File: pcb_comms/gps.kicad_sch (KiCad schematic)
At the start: 22 parts, among them U1 MAX-M10S-00B

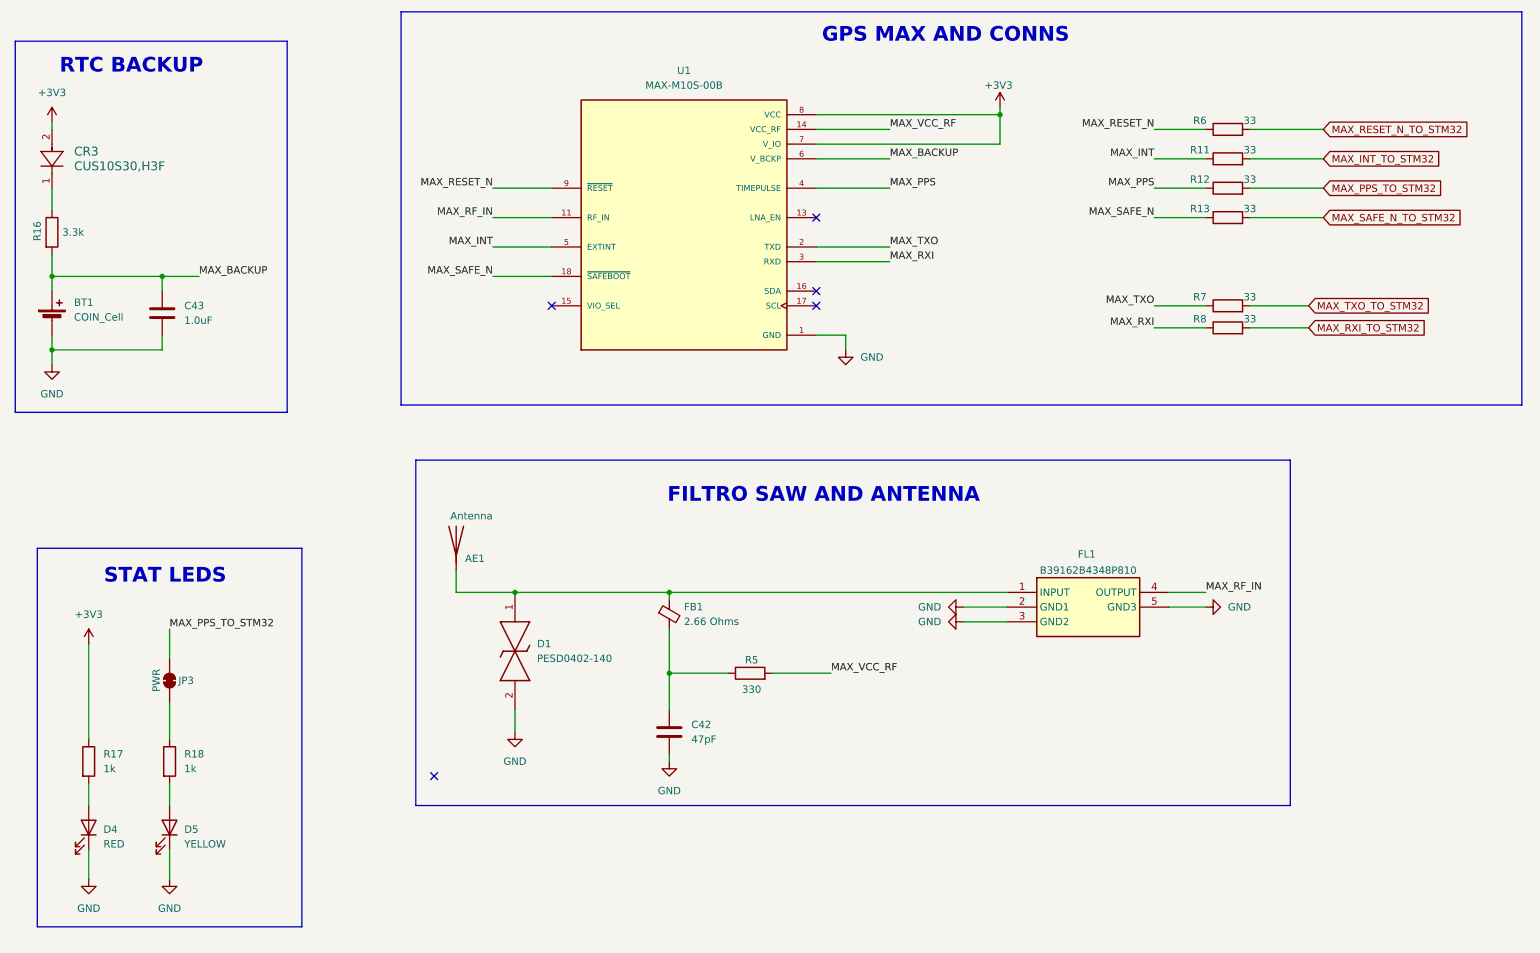
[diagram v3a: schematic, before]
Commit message: Add antenna deploy
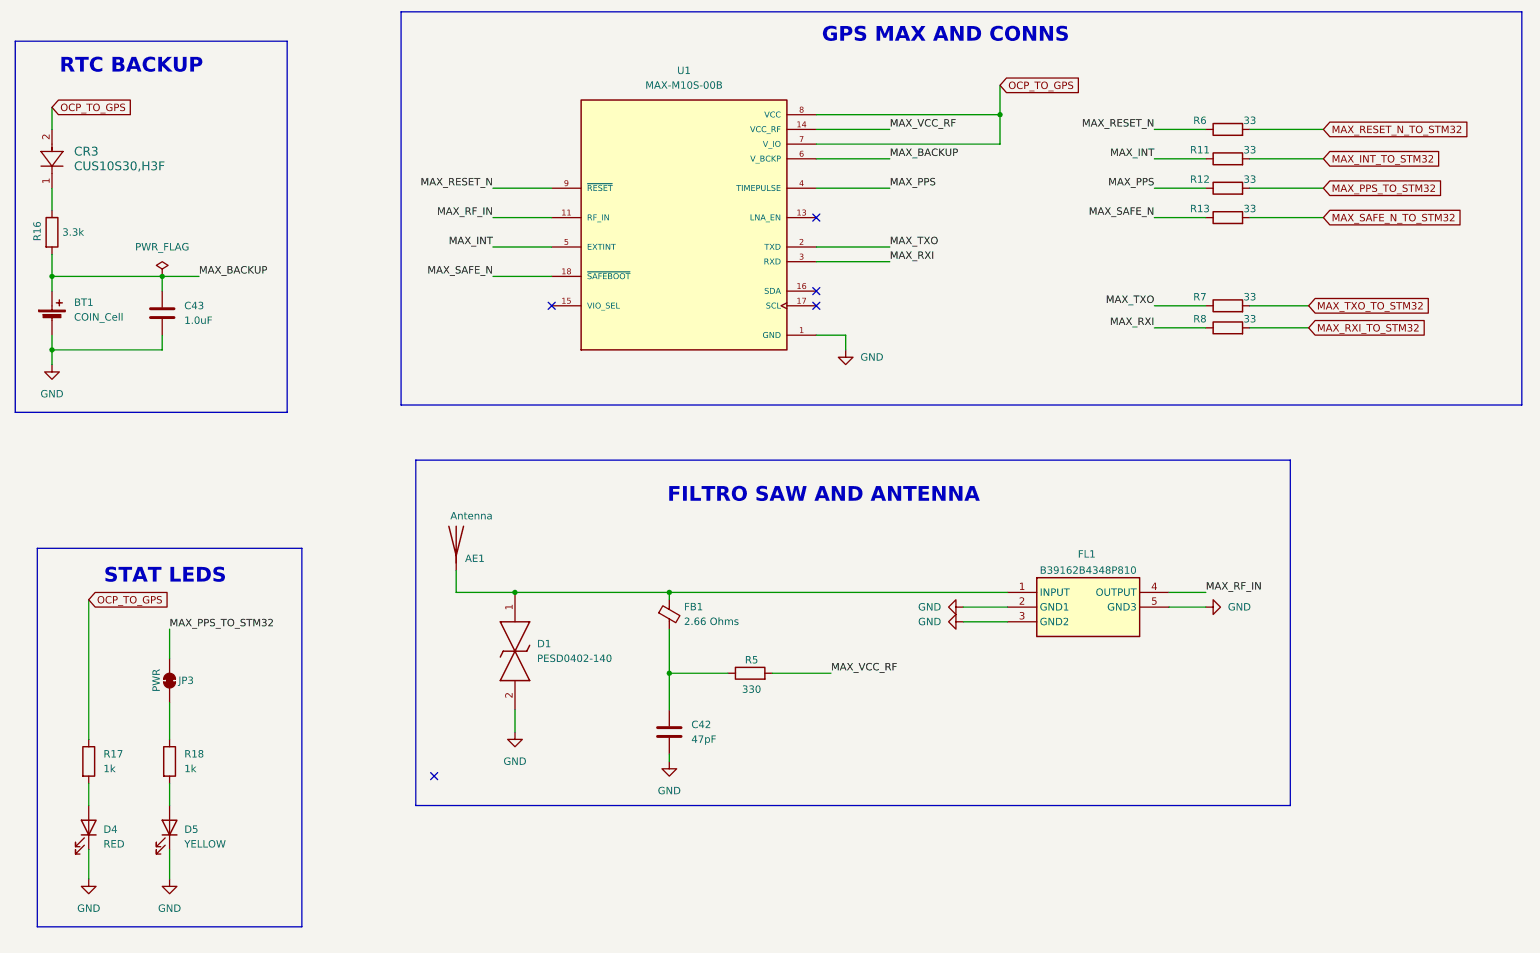
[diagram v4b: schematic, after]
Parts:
- D1: footprint DIONC1005X43N -> (none)
- FL1: footprint B39162B4348P810 -> (none)
- U1: footprint (none) -> MAX-M10S-00B:XCVR_MAX-M10S-00B
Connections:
- net +3V3 renamed OCP_TO_GPS
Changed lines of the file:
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@@
 	(wire
 		(pts
+			(xy 30.48 124.46) (xy 30.48 148.59)
+		)
+		(stroke
+			(width 0)
+			(type default)
+		)
+	)
+	(wire
+		(pts
 			(xy 187.96 45.72) (xy 187.96 40.64)
 		)
@@
 	(wire
 		(pts
-			(xy 24.13 41.91) (xy 24.13 43.18)
+			(xy 24.13 39.37) (xy 24.13 43.18)
 		)
 		(stroke
@@
 	(wire
 		(pts
-			(xy 187.96 40.64) (xy 187.96 39.37)
+			(xy 187.96 40.64) (xy 187.96 35.56)
 		)
 		(stroke
@@
 	(wire
 		(pts
-			(xy 30.48 132.08) (xy 30.48 148.59)
-		)
-		(stroke
-			(width 0)
-			(type default)
-		)
-	)
-	(wire
-		(pts
 			(xy 104.14 123.19) (xy 93.98 123.19)
 		)
@@
 		)
 	)
+	(global_label "OCP_TO_GPS"
+		(shape input)
+		(at 187.96 35.56 0)
+		(fields_autoplaced yes)
+		(effects
+			(font
+				(size 1.27 1.27)
+			)
+			(justify left)
+		)
+		(property "Intersheetrefs" "${INTERSHEET_REFS}"
+			(at 202.7985 35.56 0)
+			(effects
+				(font
+					(size 1.27 1.27)
+				)
+				(justify left)
+				(hide yes)
+			)
+		)
+	)
 	(global_label "MAX_PPS_TO_STM32"
 		(shape input)
@@
 		)
 	)
+	(global_label "OCP_TO_GPS"
+		(shape input)
+		(at 30.48 124.46 0)
+		(fields_autoplaced yes)
+		(effects
+			(font
+				(size 1.27 1.27)
+			)
+			(justify left)
+		)
+		(property "Intersheetrefs" "${INTERSHEET_REFS}"
+			(at 45.3185 124.46 0)
+			(effects
+				(font
+					(size 1.27 1.27)
+				)
+				(justify left)
+				(hide yes)
+			)
+		)
+	)
+	(global_label "OCP_TO_GPS"
+		(shape input)
+		(at 24.13 39.37 0)
+		(fields_autoplaced yes)
+		(effects
+			(font
+				(size 1.27 1.27)
+			)
+			(justify left)
+		)
+		(property "Intersheetrefs" "${INTERSHEET_REFS}"
+			(at 38.9685 39.37 0)
+			(effects
+				(font
+					(size 1.27 1.27)
+				)
+				(justify left)
+				(hide yes)
+			)
+		)
+	)
 	(global_label "MAX_TXO_TO_STM32"
 		(shape input)
@@
 	)
 	(symbol
+		(lib_id "power:PWR_FLAG")
+		(at 43.18 68.58 0)
+		(unit 1)
+		(exclude_from_sim no)
+		(in_bom yes)
+		(on_board yes)
+		(dnp no)
+		(fields_autoplaced yes)
+		(property "Reference" "#FLG07"
+			(at 43.18 66.675 0)
+			(effects
+				(font
+					(size 1.27 1.27)
+				)
+				(hide yes)
+			)
+		)
+		(property "Value" "PWR_FLAG"
+			(at 43.18 63.5 0)
+			(effects
+				(font
+					(size 1.27 1.27)
+				)
+			)
+		)
+		(property "Footprint" ""
+			(at 43.18 68.58 0)
+			(effects
+				(font
+					(size 1.27 1.27)
+				)
+				(hide yes)
+			)
+		)
+		(property "Datasheet" "~"
+			(at 43.18 68.58 0)
+			(effects
+				(font
+					(size 1.27 1.27)
+				)
+				(hide yes)
+			)
+		)
+		(property "Description" "Special symbol for telling ERC where power comes from"
+			(at 43.18 68.58 0)
+			(effects
+				(font
+					(size 1.27 1.27)
+				)
+				(hide yes)
+			)
+		)
+		(pin "1"
+		)
+		(instances
+			(project ""
+				(path "/ea597178-b44d-4db9-826c-8f86e8d231f0/9ced98fe-3695-442f-a613-f1ea774ec3ca"
+					(reference "#FLG07")
+					(unit 1)
+				)
+			)
+		)
+	)
+	(symbol
 		(lib_id "Device:R")
 		(at 144.78 137.16 90)
@@
 			)
 		)
-		(property "Footprint" "B39162B4348P810"
+		(property "Footprint" ""
 			(at 257.81 220.65 0)
 			(effects
@@
 			)
 		)
-		(property "Footprint" "DIONC1005X43N"
+		(property "Footprint" ""
 			(at 10.49 135.89 0)
 			(effects
@@
 			)
 		)
-		(property "Footprint" ""
+		(property "Footprint" "MAX-M10S-00B:XCVR_MAX-M10S-00B"
 			(at 133.35 58.42 0)
 			(effects
@@
 	)
 	(symbol
-		(lib_id "power:+3V3")
-		(at 24.13 41.91 0)
-		(unit 1)
-		(exclude_from_sim no)
-		(in_bom yes)
-		(on_board yes)
-		(dnp no)
-		(fields_autoplaced yes)
-		(property "Reference" "#PWR052"
-			(at 24.13 45.72 0)
-			(effects
-				(font
-					(size 1.27 1.27)
-				)
-				(hide yes)
-			)
-		)
-		(property "Value" "+3V3"
-			(at 24.13 36.83 0)
-			(effects
-				(font
-					(size 1.27 1.27)
-				)
-			)
-		)
-		(property "Footprint" ""
-			(at 24.13 41.91 0)
-			(effects
-				(font
-					(size 1.27 1.27)
-				)
-				(hide yes)
-			)
-		)
-		(property "Datasheet" ""
-			(at 24.13 41.91 0)
-			(effects
-				(font
-					(size 1.27 1.27)
-				)
-				(hide yes)
-			)
-		)
-		(property "Description" "Power symbol creates a global label with name \"+3V3\""
-			(at 24.13 41.91 0)
-			(effects
-				(font
-					(size 1.27 1.27)
-				)
-				(hide yes)
-			)
-		)
-		(pin "1"
-		)
-		(instances
-			(project ""
-				(path "/ea597178-b44d-4db9-826c-8f86e8d231f0/9ced98fe-3695-442f-a613-f1ea774ec3ca"
-					(reference "#PWR052")
-					(unit 1)
-				)
-			)
-		)
-	)
-	(symbol
 		(lib_id "Device:R")
 		(at 227.33 58.42 90)
@@
 	)
 	(symbol
-		(lib_id "power:+3V3")
-		(at 30.48 132.08 0)
-		(unit 1)
-		(exclude_from_sim no)
-		(in_bom yes)
-		(on_board yes)
-		(dnp no)
-		(fields_autoplaced yes)
-		(property "Reference" "#PWR054"
-			(at 30.48 135.89 0)
-			(effects
-				(font
-					(size 1.27 1.27)
-				)
-				(hide yes)
-			)
-		)
-		(property "Value" "+3V3"
-			(at 30.48 127 0)
-			(effects
-				(font
-					(size 1.27 1.27)
-				)
-			)
-		)
-		(property "Footprint" ""
-			(at 30.48 132.08 0)
-			(effects
-				(font
-					(size 1.27 1.27)
-				)
-				(hide yes)
-			)
-		)
-		(property "Datasheet" ""
-			(at 30.48 132.08 0)
-			(effects
-				(font
-					(size 1.27 1.27)
-				)
-				(hide yes)
-			)
-		)
-		(property "Description" "Power symbol creates a global label with name \"+3V3\""
-			(at 30.48 132.08 0)
-			(effects
-				(font
-					(size 1.27 1.27)
-				)
-				(hide yes)
-			)
-		)
-		(pin "1"
-		)
-		(instances
-			(project "pcb_comms_board"
-				(path "/ea597178-b44d-4db9-826c-8f86e8d231f0/9ced98fe-3695-442f-a613-f1ea774ec3ca"
-					(reference "#PWR054")
-					(unit 1)
-				)
-			)
-		)
-	)
-	(symbol
 		(lib_id "power:GND")
 		(at 223.52 125.73 90)
@@
 					(unit 1)
 				)
-			)
-		)
-	)
-	(symbol
-		(lib_id "power:+3V3")
-		(at 187.96 39.37 0)
-		(unit 1)
-		(exclude_from_sim no)
-		(in_bom yes)
-		(on_board yes)
-		(dnp no)
-		(property "Reference" "#PWR044"
-			(at 187.96 43.18 0)
-			(effects
-				(font
-					(size 1.27 1.27)
-				)
-				(hide yes)
-			)
-		)
-		(property "Value" "+3V3"
-			(at 187.706 35.56 0)
-			(effects
-				(font
-					(size 1.27 1.27)
-				)
-			)
-		)
-		(property "Footprint" ""
-			(at 187.96 39.37 0)
-			(effects
-				(font
-					(size 1.27 1.27)
-				)
-				(hide yes)
-			)
-		)
-		(property "Datasheet" ""
-			(at 187.96 39.37 0)
-			(effects
-				(font
-					(size 1.27 1.27)
-				)
-				(hide yes)
-			)
-		)
-		(property "Description" "Power symbol creates a global label with name \"+3V3\""
-			(at 187.96 39.37 0)
-			(effects
-				(font
-					(size 1.27 1.27)
-				)
-				(hide yes)
-			)
-		)
-		(pin "1"
-		)
-		(instances
-			(project ""
-				(path "/ea597178-b44d-4db9-826c-8f86e8d231f0/9ced98fe-3695-442f-a613-f1ea774ec3ca"
-					(reference "#PWR044")
-					(unit 1)
-				)

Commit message: Last update
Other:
- company: (none) -> Sanie Peralta, Alejandro Campo
- title: (none) -> PC1: APRS & GPS
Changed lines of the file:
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@@
 	(generator_version "9.0")
 	(paper "A4")
+	(title_block
+		(title "PC1: APRS & GPS")
+		(date "2026-04-01")
+		(rev "1.0")
+		(company "Sanie Peralta, Alejandro Campo")
+		(comment 1 "Introducción a la Ingeniería Satelital ")
+		(comment 2 "Primer Parcial")
+	)
 	(text "GPS MAX AND CONNS"
 		(exclude_from_sim no)

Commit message: rev 1.1
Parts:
- removed AE1: Antenna, symbol Device:Antenna
- added AE2: Antenna_Shield, symbol Device:Antenna_Shield
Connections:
- net GND: now also AE2.2 (Shield)
- net at D1.1, FB1.1, FL1.1 (INPUT): now also AE2.1 (A)
- no-connect marks 5 -> 4
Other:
- moved on the sheet: D4, D5, FB1, JP3, R17, R18

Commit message: Finish schematic
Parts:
- U1: footprint MAX-M10S-00B:XCVR_MAX-M10S-00B -> (none)
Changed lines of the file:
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@@
 	(wire
 		(pts
-			(xy 48.26 132.08) (xy 48.26 137.16)
+			(xy 48.26 130.81) (xy 48.26 137.16)
 		)
 		(stroke
@@
 		)
 	)
-	(label "MAX_PPS_TO_STM32"
-		(at 48.26 132.08 0)
-		(effects
-			(font
-				(size 1.27 1.27)
-			)
-			(justify left bottom)
-		)
-	)
 	(label "MAX_PPS"
 		(at 168.91 53.34 0)
@@
 			)
 			(justify right bottom)
+		)
+	)
+	(global_label "MAX_PPS_TO_STM32"
+		(shape input)
+		(at 48.26 130.81 0)
+		(fields_autoplaced yes)
+		(effects
+			(font
+				(size 1.27 1.27)
+			)
+			(justify left)
+		)
+		(property "Intersheetrefs" "${INTERSHEET_REFS}"
+			(at 69.9926 130.81 0)
+			(effects
+				(font
+					(size 1.27 1.27)
+				)
+				(justify left)
+				(hide yes)
+			)
 		)
 	)
@@
 			)
 		)
-		(property "Footprint" "MAX-M10S-00B:XCVR_MAX-M10S-00B"
+		(property "Footprint" ""
 			(at 133.35 58.42 0)
 			(effects

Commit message: Version 1.0. No DRA yet
From now on I will make the connections for IIS and then adapt it for the club
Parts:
- C43: value 1.0uF -> 1uF
- FB1: value 2.66 Ohms -> 2.66R
- R11, R12, R13, R6, R7, R8: value 33 -> 33R
- R16: value 3.3k -> 3.3K
- R17, R18: value 1k -> 1K
- R5: value 330 -> 330R
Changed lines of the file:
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@@
 			)
 		)
-		(property "Value" "2.66 Ohms"
+		(property "Value" "2.66R"
 			(at 133.35 130.7718 0)
 			(effects
@@
 			)
 		)
-		(property "Value" "330"
+		(property "Value" "330R"
 			(at 145.034 139.954 90)
 			(effects
@@
 			)
 		)
-		(property "Value" "33"
-			(at 231.14 51.816 90)
+		(property "Value" "33R"
+			(at 232.41 52.324 90)
 			(effects
 				(font
@@
 			)
 		)
-		(property "Value" "1k"
+		(property "Value" "1K"
 			(at 36.83 156.2099 0)
 			(effects
@@
 			)
 		)
-		(property "Value" "33"
-			(at 231.14 46.736 90)
+		(property "Value" "33R"
+			(at 232.41 47.244 90)
 			(effects
 				(font
@@
 			)
 		)
-		(property "Value" "3.3k"
+		(property "Value" "3.3K"
 			(at 25.908 60.96 0)
 			(effects
@@
 			)
 		)
-		(property "Value" "1k"
+		(property "Value" "1K"
 			(at 50.8 156.2099 0)
 			(effects
@@
 			)
 		)
-		(property "Value" "33"
-			(at 231.14 41.656 90)
+		(property "Value" "33R"
+			(at 232.41 41.656 90)
 			(effects
 				(font
@@
 			)
 		)
-		(property "Value" "1.0uF"
+		(property "Value" "1uF"
 			(at 46.99 76.1999 0)
 			(effects
@@
 			)
 		)
-		(property "Value" "33"
-			(at 231.14 75.946 90)
+		(property "Value" "33R"
+			(at 232.41 76.454 90)
 			(effects
 				(font
@@
 			)
 		)
-		(property "Value" "33"
-			(at 231.14 56.896 90)
+		(property "Value" "33R"
+			(at 232.41 57.404 90)
 			(effects
 				(font
@@
 			)
 		)
-		(property "Value" "33"
-			(at 231.14 72.136 90)
-			(effects
-				(font
+		(property "Value" "33R"
+			(at 232.41 72.644 90)
+			(effects
+				(font
